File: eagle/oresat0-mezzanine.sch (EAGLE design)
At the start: 22 parts, among them U1 QBA-07+, U2 QBA-07+, U3 QBA-07+, U7 QCN-XXX+, U8 QCN-XXX+, U9 QCN-XXX+

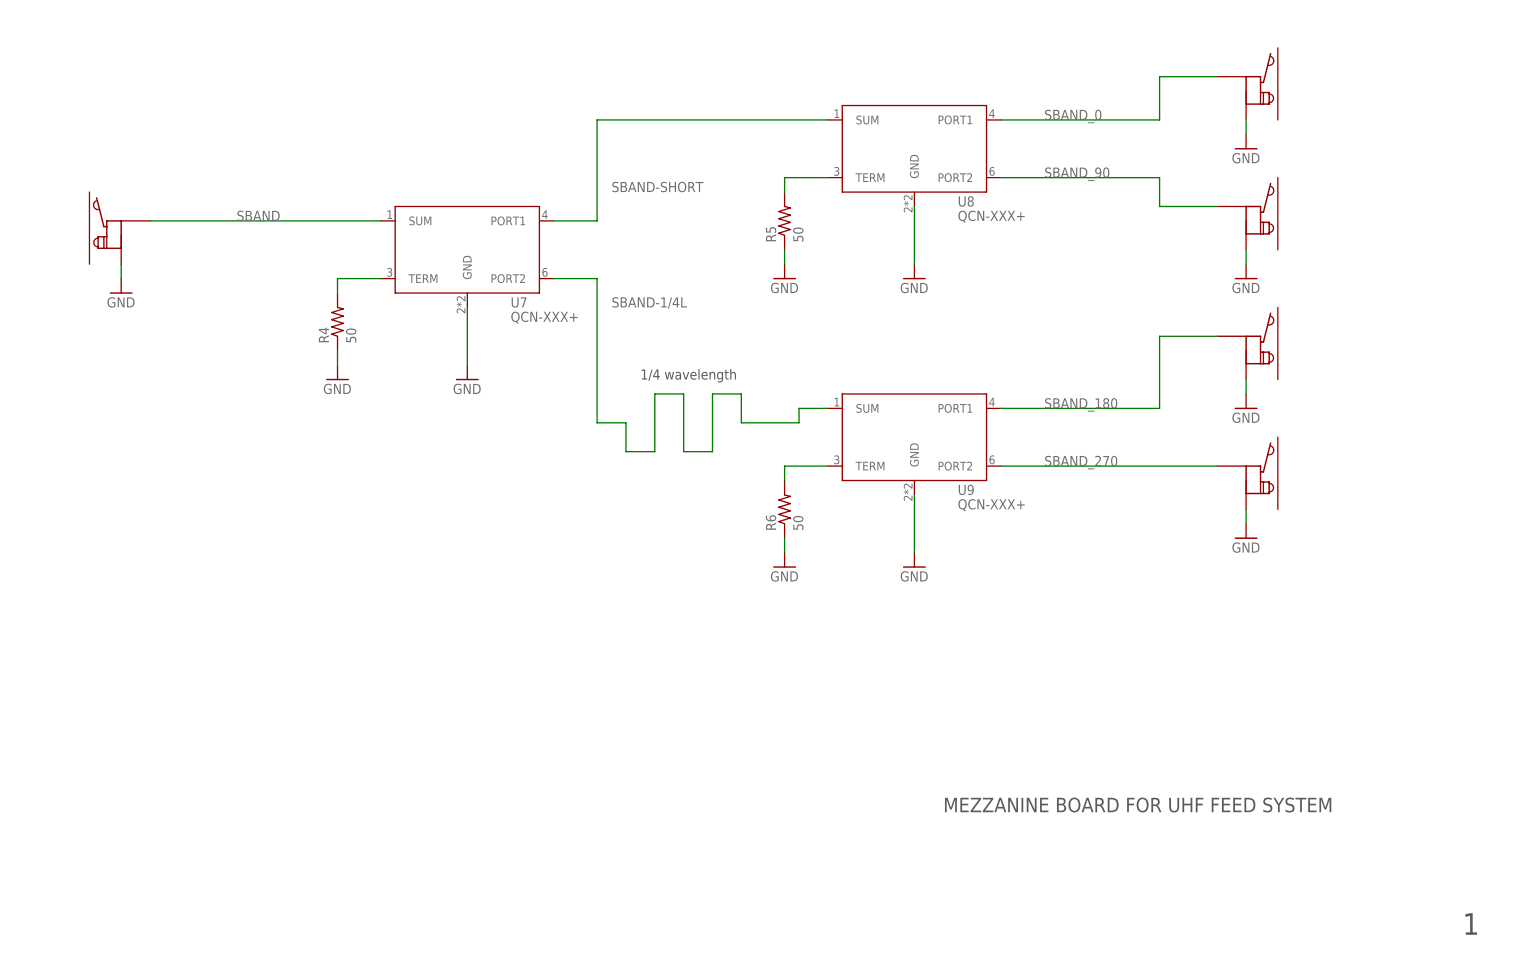
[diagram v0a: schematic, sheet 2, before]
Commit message: Final cleanup and polish of v1.1 OreSat0 +Z end card and mezzanine. Fixed S band 1/4 wave, lots of stiching and polish, fixed radial TCREAM on the contact pads, lots of TNAMES polish.
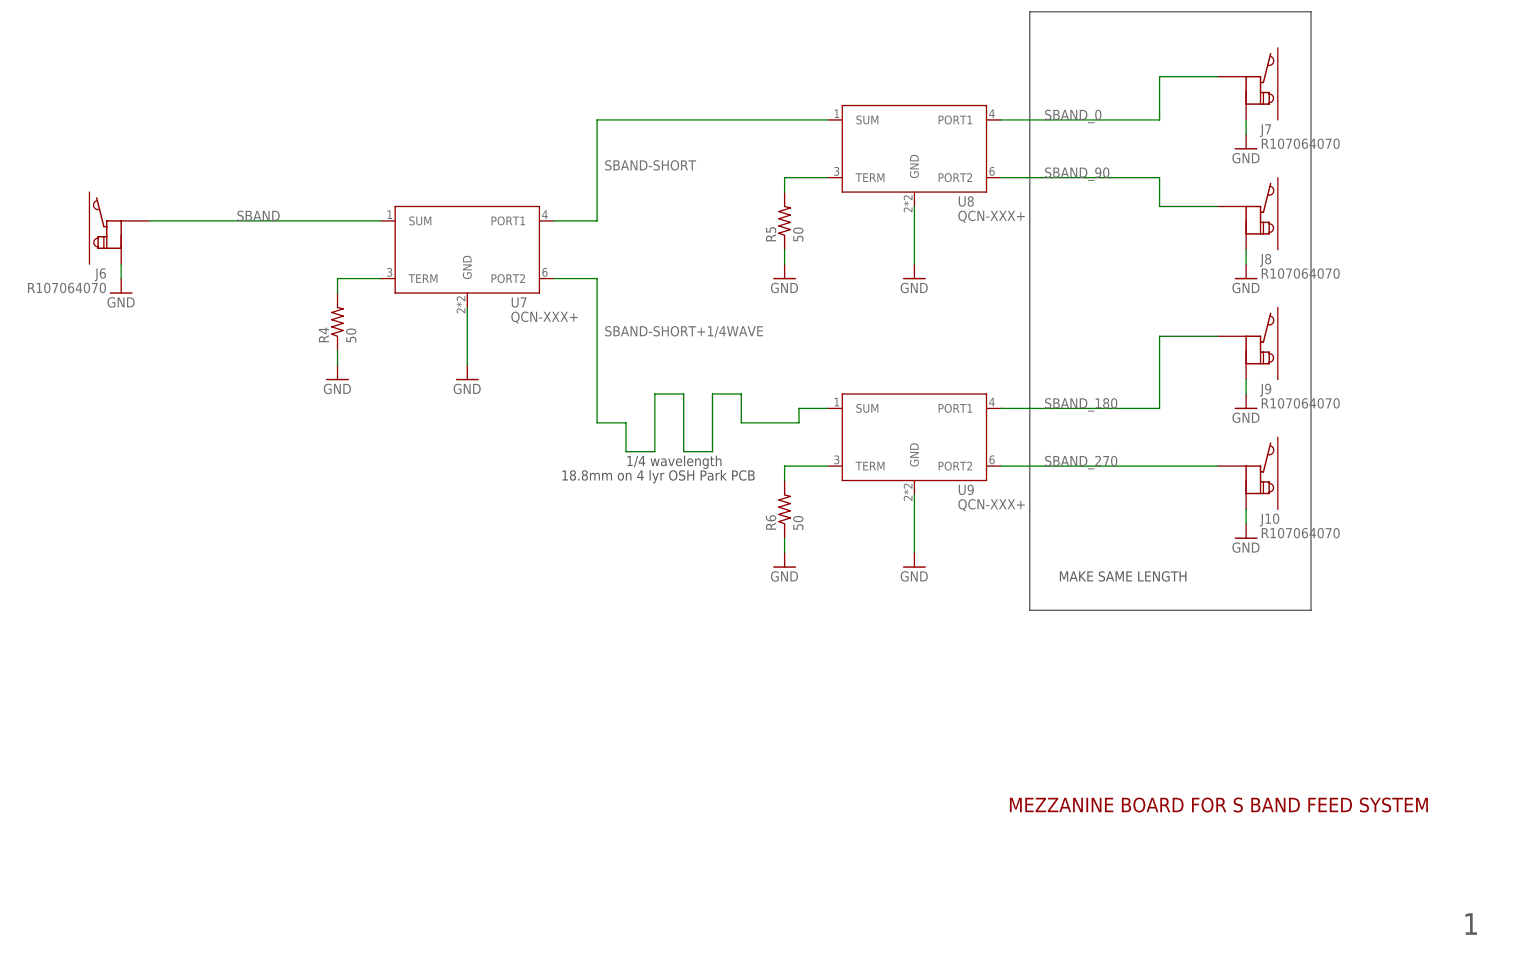
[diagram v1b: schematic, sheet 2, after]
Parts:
- renumbered U$1 to J1, U$10 to J10, U$2 to J2, U$3 to J3, U$4 to J5, U$5 to J4, U$6 to J6, U$7 to J7, U$8 to J8, U$9 to J9
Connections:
- net SBAND-1/4L renamed SBAND-SHORT+1/4WAVE
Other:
- note added: "18.8mm on 4 lyr OSH Park PCB"
- note added: "MAKE SAME LENGTH"
- note added: "MEZZANINE BOARD FOR S BAND FEED SYSTEM"

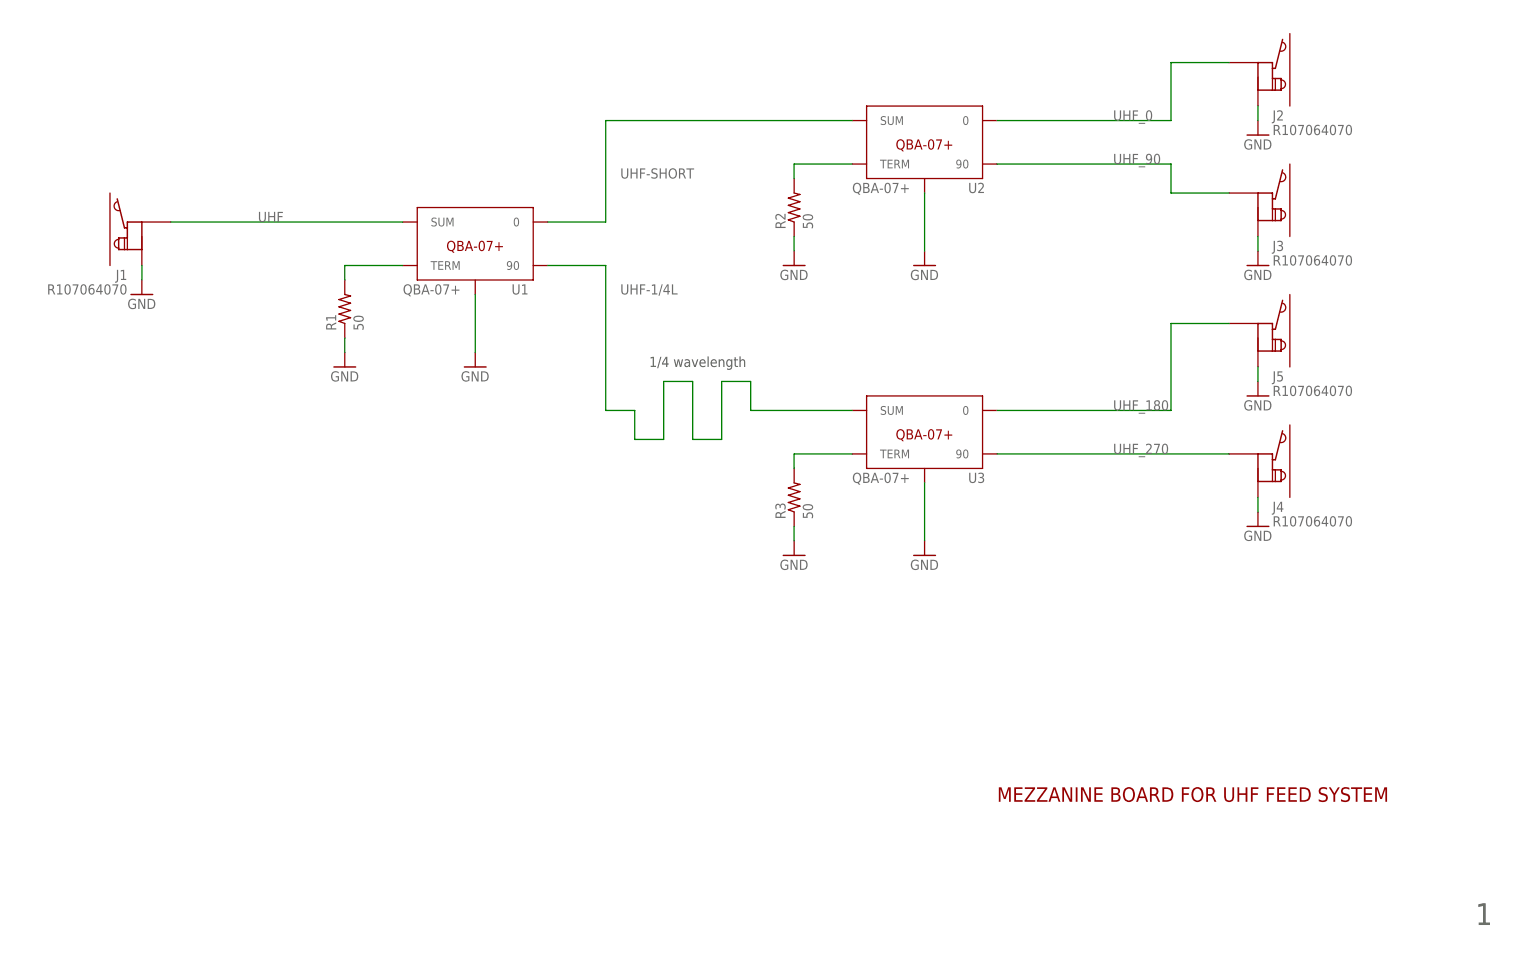
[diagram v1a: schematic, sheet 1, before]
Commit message: Clean up BOM and part numbers. Ready for v1.1 fab.
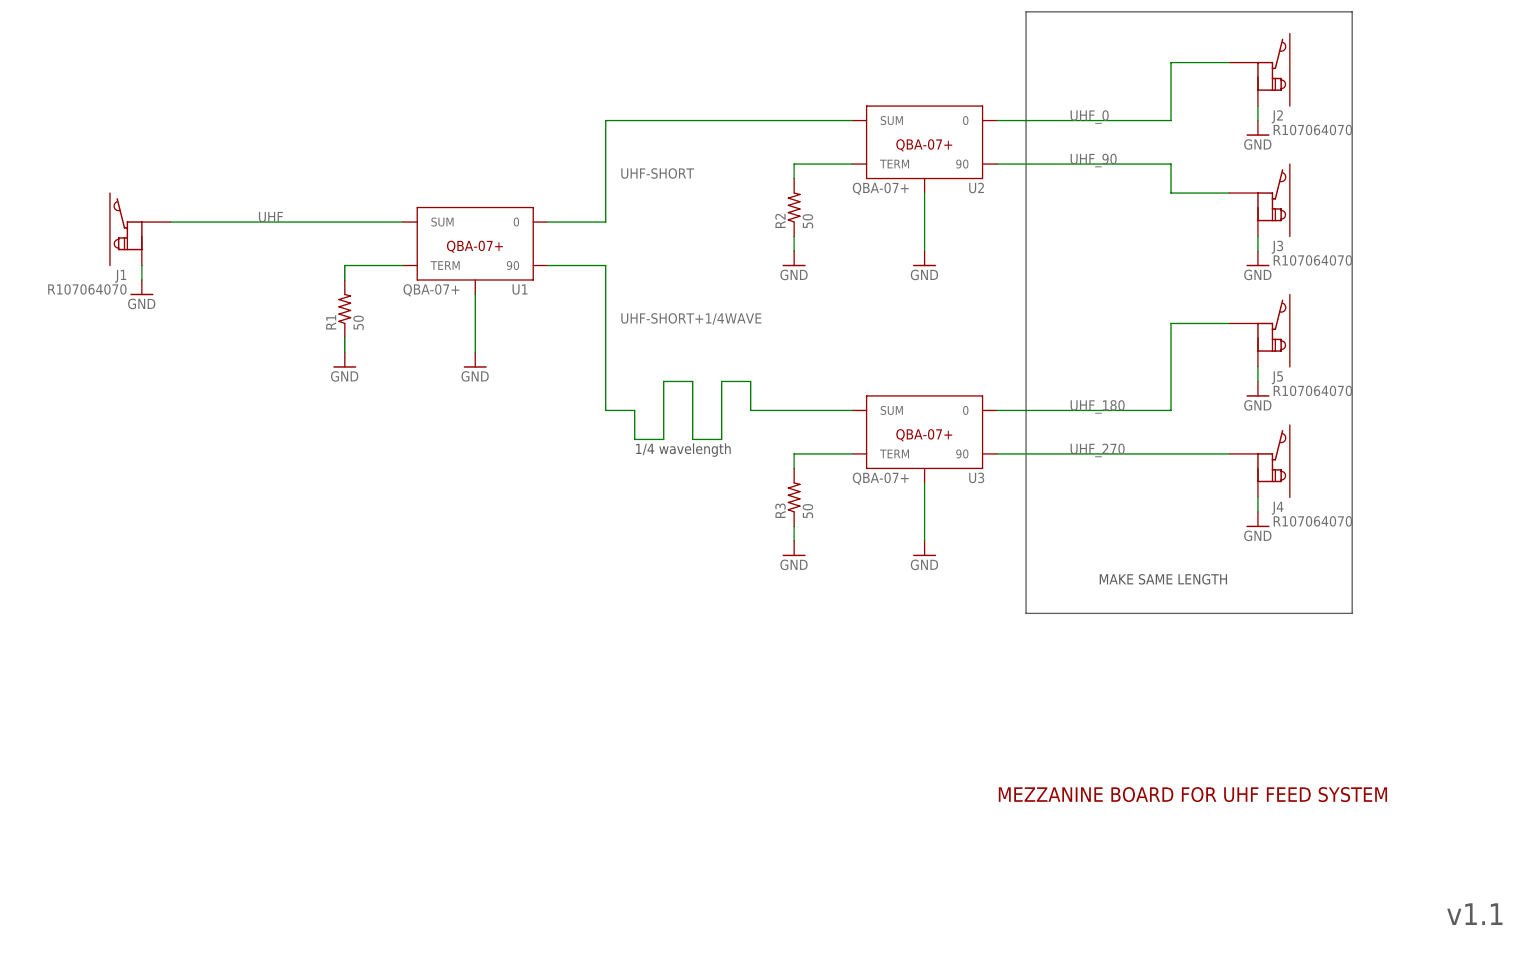
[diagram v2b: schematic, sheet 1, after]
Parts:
- U7, U8, U9: value QCN-XXX+ -> QCN-27+
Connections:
- net UHF-1/4L renamed UHF-SHORT+1/4WAVE
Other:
- note added: "v1.1"
- note removed: "1"

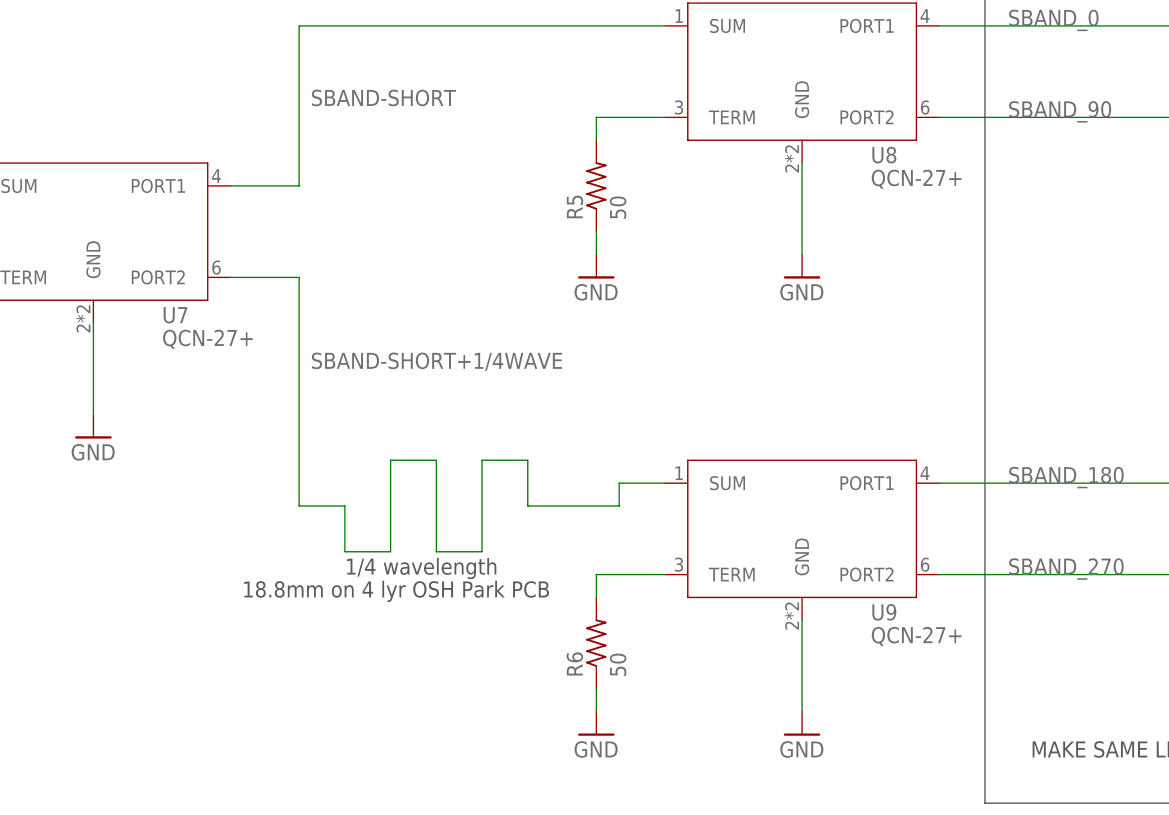
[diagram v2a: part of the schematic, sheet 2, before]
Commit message: Switched to a QCN-27D+ (with DC passthrough) for S band, and made the U and L band 1/4 wave lengths a bit more precise after getting precise lengths from Eric.
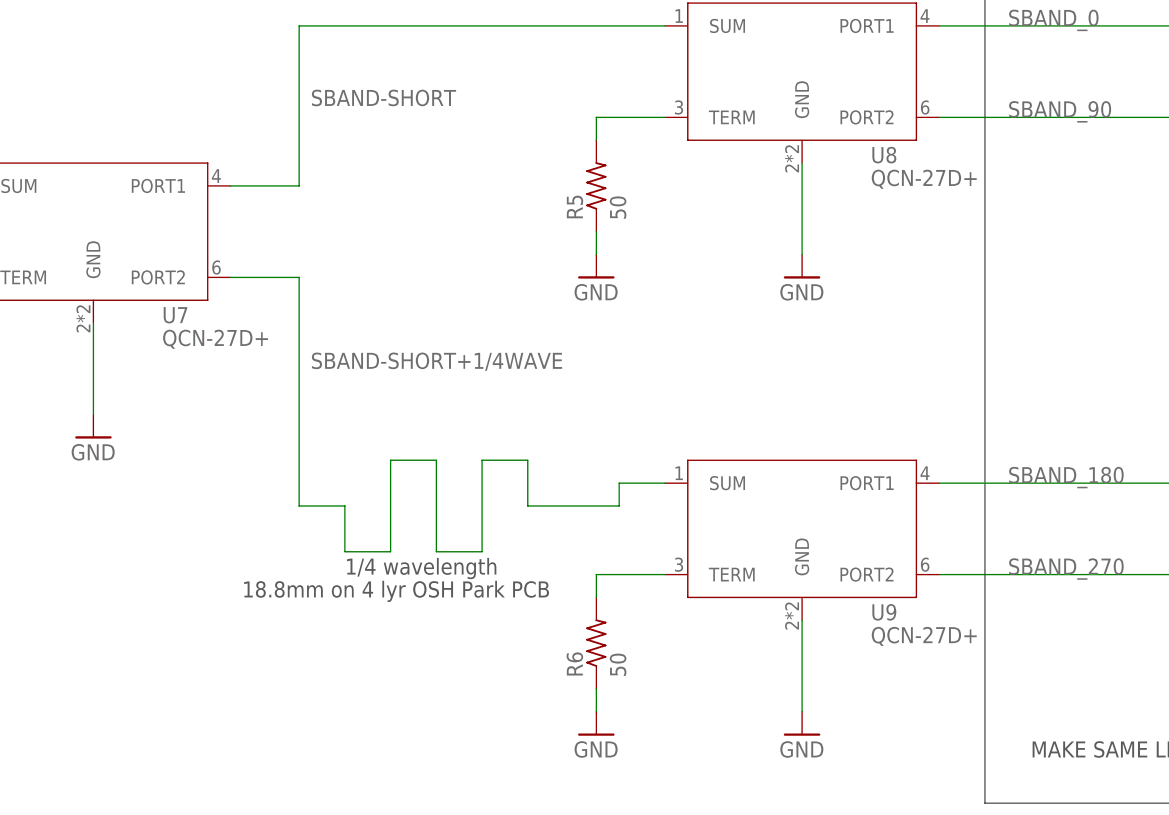
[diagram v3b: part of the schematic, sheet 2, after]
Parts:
- U7, U8, U9: value QCN-27+ -> QCN-27D+
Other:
- note added: "105 mm on 4 lyr OSH Park PCB"
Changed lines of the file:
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@@
 <part name="J9" library="J-Radiall-R107064070-RF" deviceset="R107064070" device=""/>
 <part name="J10" library="J-Radiall-R107064070-RF" deviceset="R107064070" device=""/>
-<part name="U7" library="U-MiniCirc-QCN-XXX+-quad" deviceset="QCN-XXX+" device="" value="QCN-27+"/>
-<part name="U8" library="U-MiniCirc-QCN-XXX+-quad" deviceset="QCN-XXX+" device="" value="QCN-27+"/>
-<part name="U9" library="U-MiniCirc-QCN-XXX+-quad" deviceset="QCN-XXX+" device="" value="QCN-27+"/>
+<part name="U7" library="U-MiniCirc-QCN-XXX+-quad" deviceset="QCN-XXX+" device="" value="QCN-27D+"/>
+<part name="U8" library="U-MiniCirc-QCN-XXX+-quad" deviceset="QCN-XXX+" device="" value="QCN-27D+"/>
+<part name="U9" library="U-MiniCirc-QCN-XXX+-quad" deviceset="QCN-XXX+" device="" value="QCN-27D+"/>
 </parts>
 <sheets>
@@
 <wire x1="245.11" y1="166.37" x2="187.96" y2="166.37" width="0.1524" layer="97"/>
 <wire x1="187.96" y1="166.37" x2="187.96" y2="60.96" width="0.1524" layer="97"/>
+<text x="109.22" y="86.36" size="1.778" layer="97">105 mm on 4 lyr OSH Park PCB</text>
 </plain>
 <instances>

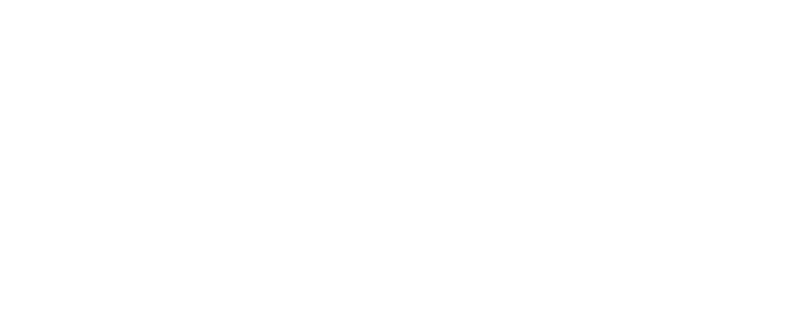
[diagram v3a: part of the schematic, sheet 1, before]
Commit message: Small tweaks; reduced mezanine board size. Added flight tags. Off to fab!
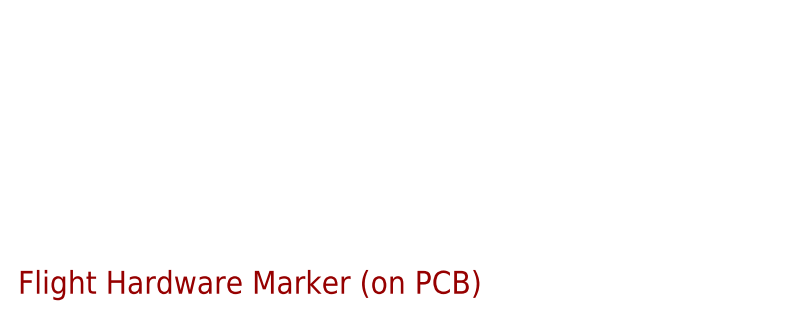
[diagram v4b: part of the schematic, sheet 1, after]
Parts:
- added U$1: FLIGHMARKERNEW, oresat-flight-marker:FLIGHMARKERNEW
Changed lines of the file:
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@@
 <part name="U8" library="U-MiniCirc-QCN-XXX+-quad" deviceset="QCN-XXX+" device="" value="QCN-27D+"/>
 <part name="U9" library="U-MiniCirc-QCN-XXX+-quad" deviceset="QCN-XXX+" device="" value="QCN-27D+"/>
+<part name="U$1" library="oresat-flight-marker" deviceset="FLIGHMARKER" device="NEW"/>
 </parts>
 <sheets>
@@
 <attribute name="VALUE" x="231.14" y="76.2" size="1.778" layer="96"/>
 </instance>
+<instance part="U$1" gate="G$1" x="10.16" y="2.54" smashed="yes"/>
 </instances>
 <busses>
